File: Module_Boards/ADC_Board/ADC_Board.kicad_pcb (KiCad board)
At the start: 6 copper layers, 15.6 x 19.7 mm, 74 parts, among them J1 212134-0003, J2 212134-0003, J3 212134-0003, J4 212134-0003, U1 ADS8860IDRCT, U2 REF35250YBHR, U3 TPS22916CYFPR, U4 TPS7A9401DSCR, U5 TMUX1104DQAR, U6 LTC6255IDC#TRMPBF, U7 OPA310SIDBVR, U8 OPA333AIDBVR

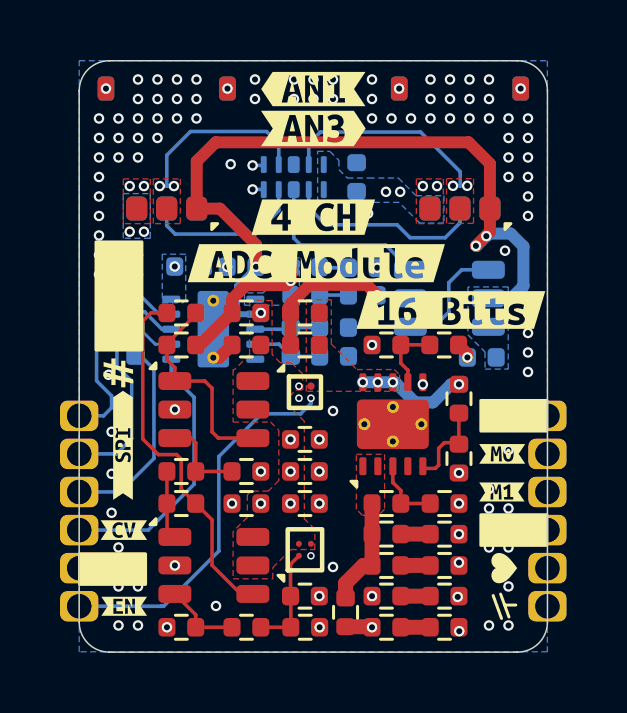
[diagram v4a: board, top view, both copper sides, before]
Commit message: Added fabrication panel. Now with latest designs
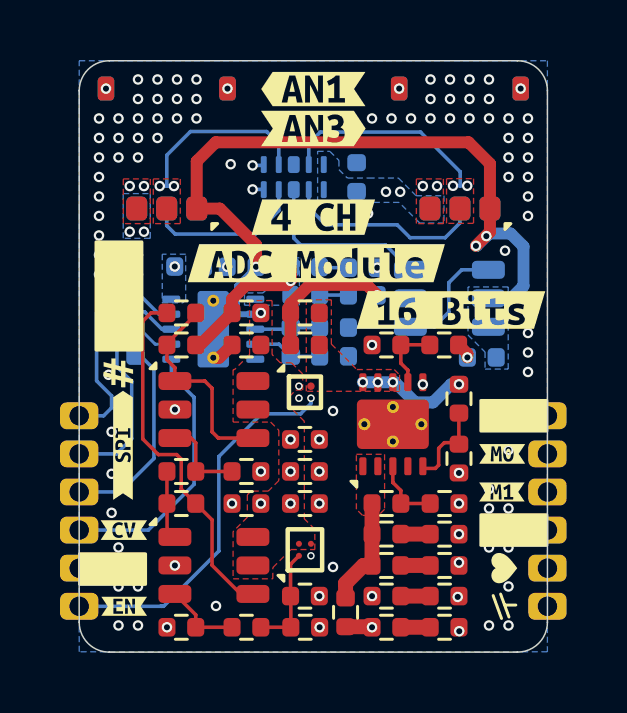
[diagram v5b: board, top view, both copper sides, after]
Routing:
- net GND: vias 136 -> 121
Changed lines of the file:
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@@
 		(pad "1" thru_hole roundrect
 			(at -7.804081 2.878 90)
-			(size 1.02 1.28)
-			(drill 0.82)
+			(size 0.9 1.28)
+			(drill 0.65)
 			(property pad_prop_castellated)
 			(layers "*.Cu" "*.Mask")
@@
 		(pad "2" thru_hole roundrect
 			(at -7.804081 4.148 90)
-			(size 1.02 1.28)
-			(drill 0.82)
+			(size 0.9 1.28)
+			(drill 0.65)
 			(property pad_prop_castellated)
 			(layers "*.Cu" "*.Mask")
@@
 		(pad "3" thru_hole roundrect
 			(at -7.804081 5.418 90)
-			(size 1.02 1.28)
-			(drill 0.82)
+			(size 0.9 1.28)
+			(drill 0.65)
 			(property pad_prop_castellated)
 			(layers "*.Cu" "*.Mask")
@@
 		(pad "4" thru_hole roundrect
 			(at -7.804081 6.688 90)
-			(size 1.02 1.28)
-			(drill 0.82)
+			(size 0.9 1.28)
+			(drill 0.65)
 			(property pad_prop_castellated)
 			(layers "*.Cu" "*.Mask")
@@
 		(pad "5" thru_hole roundrect
 			(at -7.804081 7.958 90)
-			(size 1.02 1.28)
-			(drill 0.82)
+			(size 0.9 1.28)
+			(drill 0.65)
 			(property pad_prop_castellated)
 			(layers "*.Cu" "*.Mask")
@@
 		(pad "6" thru_hole roundrect
 			(at -7.804081 9.228 90)
-			(size 1.02 1.28)
-			(drill 0.82)
+			(size 0.9 1.28)
+			(drill 0.65)
 			(property pad_prop_castellated)
 			(layers "*.Cu" "*.Mask")
@@
 		(pad "7" thru_hole roundrect
 			(at 7.804081 9.228 90)
-			(size 1.02 1.28)
-			(drill 0.82)
+			(size 0.9 1.28)
+			(drill 0.65)
 			(property pad_prop_castellated)
 			(layers "*.Cu" "*.Mask")
@@
 		(pad "8" thru_hole roundrect
 			(at 7.804081 7.958 90)
-			(size 1.02 1.28)
-			(drill 0.82)
+			(size 0.9 1.28)
+			(drill 0.65)
 			(property pad_prop_castellated)
 			(layers "*.Cu" "*.Mask")
@@
 		(pad "9" thru_hole roundrect
 			(at 7.804081 6.688 90)
-			(size 1.02 1.28)
-			(drill 0.82)
+			(size 0.9 1.28)
+			(drill 0.65)
 			(property pad_prop_castellated)
 			(layers "*.Cu" "*.Mask")
@@
 		(pad "10" thru_hole roundrect
 			(at 7.804081 5.418 90)
-			(size 1.02 1.28)
-			(drill 0.82)
+			(size 0.9 1.28)
+			(drill 0.65)
 			(property pad_prop_castellated)
 			(layers "*.Cu" "*.Mask")
@@
 		(pad "11" thru_hole roundrect
 			(at 7.804081 4.148 90)
-			(size 1.02 1.28)
-			(drill 0.82)
+			(size 0.9 1.28)
+			(drill 0.65)
 			(property pad_prop_castellated)
 			(layers "*.Cu" "*.Mask")
@@
 		(pad "12" thru_hole roundrect
 			(at 7.804081 2.878 90)
-			(size 1.02 1.28)
-			(drill 0.82)
+			(size 0.9 1.28)
+			(drill 0.65)
 			(property pad_prop_castellated)
 			(layers "*.Cu" "*.Mask")
@@
 			)
 		)
+		(property "MPN" "TPS7A9401DSCR"
+			(at 0 0 90)
+			(unlocked yes)
+			(layer "F.Fab")
+			(hide yes)
+			(effects
+				(font
+					(size 1 1)
+					(thickness 0.15)
+				)
+			)
+		)
 		(sheetname "[1] Power Regulation & Connectors")
 		(sheetfile "[1] Power Regulation & Connectors.kicad_sch")
@@
 	)
 	(via
-		(at 133.780419 70.905328)
-		(size 0.35)
-		(drill 0.2)
-		(layers "F.Cu" "B.Cu")
-		(free yes)
-		(net 2)
-	)
-	(via
 		(at 141.580419 84.555328)
 		(size 0.35)
@@
 	)
 	(via
-		(at 137.680419 70.905328)
-		(size 0.35)
-		(drill 0.2)
-		(layers "F.Cu" "B.Cu")
-		(free yes)
-		(net 2)
-	)
-	(via
 		(at 139.630419 71.555328)
 		(size 0.35)
@@
 	)
 	(via
-		(at 137.030419 71.555328)
-		(size 0.35)
-		(drill 0.2)
-		(layers "F.Cu" "B.Cu")
-		(free yes)
-		(net 2)
-	)
-	(via
 		(at 140.578922 83.371678)
 		(size 0.35)
@@
 	)
 	(via
-		(at 137.030419 70.905328)
-		(size 0.35)
-		(drill 0.2)
-		(layers "F.Cu" "B.Cu")
-		(free yes)
-		(net 2)
-	)
-	(via
 		(at 142.230419 82.605328)
 		(size 0.35)
@@
 	)
 	(via
-		(at 135.080419 70.255328)
-		(size 0.35)
-		(drill 0.2)
-		(layers "F.Cu" "B.Cu")
-		(free yes)
-		(net 2)
-	)
-	(via
 		(at 129.880419 72.205328)
 		(size 0.35)
@@
 	)
 	(via
-		(at 133.780419 70.255328)
-		(size 0.35)
-		(drill 0.2)
-		(layers "F.Cu" "B.Cu")
-		(free yes)
-		(net 2)
-	)
-	(via
-		(at 135.730419 70.905328)
-		(size 0.35)
-		(drill 0.2)
-		(layers "F.Cu" "B.Cu")
-		(free yes)
-		(net 2)
-	)
-	(via
-		(at 134.430419 70.255328)
-		(size 0.35)
-		(drill 0.2)
-		(layers "F.Cu" "B.Cu")
-		(free yes)
-		(net 2)
-	)
-	(via
 		(at 135.925 84.390278)
 		(size 0.35)
@@
 	)
 	(via
-		(at 137.680419 70.255328)
-		(size 0.35)
-		(drill 0.2)
-		(layers "F.Cu" "B.Cu")
-		(free yes)
-		(net 2)
-	)
-	(via
 		(at 131.830419 70.255328)
 		(size 0.35)
@@
 	)
 	(via
-		(at 136.380419 70.905328)
-		(size 0.35)
-		(drill 0.2)
-		(layers "F.Cu" "B.Cu")
-		(free yes)
-		(net 2)
-	)
-	(via
 		(at 131.11 86.454878)
 		(size 0.35)
@@
 	)
 	(via
-		(at 135.080419 70.905328)
-		(size 0.35)
-		(drill 0.2)
-		(layers "F.Cu" "B.Cu")
-		(free yes)
-		(net 2)
-	)
-	(via
 		(at 129 82)
 		(size 0.35)
@@
 	)
 	(via
-		(at 135.730419 70.255328)
-		(size 0.35)
-		(drill 0.2)
-		(layers "F.Cu" "B.Cu")
-		(free yes)
-		(net 2)
-	)
-	(via
 		(at 132.863 70.5596)
 		(size 0.35)
@@
 	)
 	(via
-		(at 134.430419 70.905328)
-		(size 0.35)
-		(drill 0.2)
-		(layers "F.Cu" "B.Cu")
-		(free yes)
-		(net 2)
-	)
-	(via
 		(at 130.530419 71.555328)
 		(size 0.35)
@@
 	)
 	(via
-		(at 136.380419 70.255328)
-		(size 0.35)
-		(drill 0.2)
-		(layers "F.Cu" "B.Cu")
-		(free yes)
-		(net 2)
-	)
-	(via
 		(at 129.880419 86.505328)
 		(size 0.35)
@@
 	)
 	(via
-		(at 137.030419 70.255328)
-		(size 0.35)
-		(drill 0.2)
-		(layers "F.Cu" "B.Cu")
-		(free yes)
-		(net 2)
-	)
-	(via
 		(at 140.5382 87.503)
 		(size 0.35)
@@
 		)
 	)
-	(group "ViaStitching GND"
-		(members "01c2a67b-ff23-47a3-adb6-5c121a9eee78" "02bf1dc9-1682-450d-9e89-dad262860b05"
-			"0418d074-8c34-4096-8f03-c06f9e5c6762" "05fe64f7-4e83-44bd-af3f-92de9346a62d"
-			"09bf9225-dbe8-45be-95a4-9c0749d707a2" "09c93011-024f-4732-b358-ce6eb8486aa9"
-			"0a28e657-61bc-492d-bbd1-ef88563191e8" "100fdaf4-bddb-4df4-99c3-21c26d49b035"
-			"11c639ab-e2a6-4a05-86d4-c0175dd8f678" "1b9682ca-97b3-4183-9a82-39c9359373ef"
-			"1f8442fa-8c0e-418c-b6e9-573842e3eabb" "2355a6e2-3cbd-44a1-9f38-631ad3c40849"
-			"23866087-b80e-46fa-bd19-d1cbb6531fae" "24f60bed-8ae6-4f8b-8e6a-1042e90808a6"
-			"272f1e89-a6d0-4e72-a52a-68f4eb4a436e" "280c459c-1ac1-4697-bf76-b9cc990e1851"
-			"2a441c19-4ee3-489e-84c1-ce4197bf9964" "3084ca1b-8e37-4e5f-bcc4-49a796856d51"
-			"347cac8b-1b62-427f-bf57-5cf12dc8047a" "35e27be1-1e39-487a-b072-c2cdfa98e90b"
-			"38ac1818-0015-4d9a-b44a-9ed3deb02b2b" "3abdee33-cc5e-4e97-ac46-a42471185ac3"
-			"3fabe065-ef5d-49c9-aaec-fa659fd30faa" "419c0ac0-2385-4cbe-99d0-338dac801893"
-			"42917181-78e5-42ae-a0fb-cbaaf0d016e3" "4c43a8c4-9dec-42c9-9366-0c37183d1633"
-			"4d5daad4-2064-4f53-b4b7-d06267b0820b" "4f3bf699-49a4-4c8d-bba2-6143a33c0b20"
-			"4faff1e4-035f-404e-b2fe-c488a2fae909" "51d10b77-9ee8-44ae-86e4-d18b244778c4"
-			"537f9e91-3c18-43a7-94c0-eb61cadda7c0" "54adabb0-60c4-45c2-b507-0bb8d61e9677"
-			"551feb6b-0cae-45d5-87f7-8e85ebc38ebc" "583a18de-cc02-415f-ad01-63d0bd5f342f"
-			"58fe4660-82da-4079-a510-6b2b84b99b6d" "599dab8d-4ce7-468e-ae49-0001d0039fb3"
-			"5bda0d59-85fe-435e-a547-eb8fcde9ed75" "5c459709-3e60-4a46-8f2b-0ab7f513110d"
-			"5fc66451-9e45-42c6-816e-37ab698be2dd" "67343714-db02-4b6a-8f50-13eaa6485fb8"
-			"6c76d681-26eb-4609-be52-1afb3b94a0e7" "6dc1e49e-3959-469f-b198-3586e5cf390e"
-			"72e197dc-11bd-4ed5-9094-221934cc369b" "737483b7-1d74-4925-a131-88b34b9fe8e1"
-			"784d38a6-5bfd-4b4b-9ec3-4d891c6d17e4" "7c64005f-3c5d-4d86-9acf-a6977f345fbf"
-			"7ca94a63-35bf-42f8-8d37-ac3e305b0694" "817633f6-cd84-47b1-81d5-0d39e99de915"
-			"8202786e-79c3-4343-9b66-7101c877622e" "823b3854-864a-4973-90dd-ec8228dd58a4"
-			"8a66695f-b23a-4ed7-a23f-1e0966ed6d87" "8c84802e-d6d7-40fe-ae19-3f10aa03ab49"
-			"90a7e8d6-6bec-47ec-825e-be0f2097b5c3" "95a61d8f-633d-4a8f-a202-29b0f7d8f06d"
-			"96860cb5-c7dd-445d-bac2-3260cc75958b" "98116d76-d377-4bb8-945b-5098d76c19a9"
-			"9c145c74-1182-4ce1-902b-baa53fa376f0" "9f0619bf-b43c-4bfa-97d3-ecb2b876e878"
-			"9f9ae469-4230-4051-8515-f45d82b9bab5" "a065066a-3d42-4698-88cf-5de5992e7068"
-			"a5f8ebb8-9813-4d4c-b212-5a993a968bdc" "aa0e437d-e1ad-4b54-8862-c58055638030"
-			"abdbb2f4-cc92-40d4-bca6-b36ec8bb2538" "b02b0c6c-5397-47fa-867b-2bc8e86fa90d"
-			"b21fbfbf-44a2-4d5d-88ba-b208d1d49c73" "b3188c8d-c565-4bda-ace1-7d007c31c58c"
-			"b59fa9ee-71d3-4603-93b1-0144bb8f1374" "b6fd1190-8fd2-4cee-b5c5-d6184795e1c6"
-			"b7d00381-067e-4121-833e-4356cffbdca3" "c2cbbe9d-15d0-42a5-aa6f-8e4689ed24c8"
-			"c3f9ea74-bb9a-49c7-ab09-5f3803fd2623" "c4f8032c-36e0-42d9-90cb-3a106a74de61"
-			"c7d35e3f-ad99-4c40-ad9b-78e2d5861aa2" "cd74da6c-a39a-4407-9375-e17365a94645"
-			"d032d956-cad2-4b7f-b5ac-024c2335ced2" "d1604600-54a3-42f5-a643-182a7ac1d4ca"
-			"d4114ba5-9790-491c-a594-0dafd517b2f5" "d871d4fe-1fcc-40c8-b8a0-ab949039d886"
-			"d93242f1-2d11-4c15-9650-50092a66d22e" "da37e09c-0e0d-48c0-9906-9950303dbce8"
-			"dcc2a7df-a0dd-45eb-b3ad-1710e57bc7fc" "dd38eb3a-e310-4b67-abda-48825d4e1d97"
-			"de8e85e9-63a1-4527-b55a-9430496be11d" "e2108a99-b6af-46c3-bbe1-736555905193"
-			"e23768f1-a068-4a87-b435-2c2aba7d2028" "e4637efc-6be3-4f98-bccb-214969b47c62"
-			"e57ae1f0-316f-46bb-b6ee-d299aee603be" "e5bb44af-8af2-4042-8452-a1da0a4982f2"
-			"e60948fc-2bd4-4695-80f9-d8c0265f2ef8" "ea5cf7a0-3c6d-467f-8739-f899da2aaef5"
-			"ea658520-571e-4e1e-958d-deeff3350253" "ea82d782-fe1f-4a58-a28c-827294517db6"
-			"ebf2694c-479e-4e91-b78f-c9883632baec" "ee5b12cb-c681-4a33-ba24-a683c90f299a"
-			"f6d25049-7cac-4876-9644-a5a45a292f5f" "fba9640a-bbb4-417b-be19-6bc927acc75e"
-		)
-	)
